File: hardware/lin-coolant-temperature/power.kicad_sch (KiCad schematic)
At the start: 22 parts, among them U4 LTC3203BEDD-PBF, U5 BD9G341EFJ

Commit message: Add firmware for lin-coolant-temperature, cleanup layout
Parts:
- renumbered D2 to D3, R10 to R11, R11 to R12, R12 to R13, R13 to R14, R14 to R15, R15 to R16, R16 to R17, R17 to R18
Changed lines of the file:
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@@
   (symbol (lib_id "power:GND") (at 144.145 89.789 0) (unit 1)
     (in_bom yes) (on_board yes) (fields_autoplaced)
-    (property "Reference" "#PWR030" (id 0) (at 144.145 96.139 0)
+    (property "Reference" "#PWR031" (id 0) (at 144.145 96.139 0)
       (effects (font (size 1.27 1.27)) hide)
     )
@@
   (symbol (lib_id "power:+3V3") (at 100.457 116.967 0) (unit 1)
     (in_bom yes) (on_board yes) (fields_autoplaced)
-    (property "Reference" "#PWR024" (id 0) (at 100.457 120.777 0)
+    (property "Reference" "#PWR025" (id 0) (at 100.457 120.777 0)
       (effects (font (size 1.27 1.27)) hide)
     )
@@
   (symbol (lib_id "power:GND") (at 100.457 152.4 0) (unit 1)
     (in_bom yes) (on_board yes) (fields_autoplaced)
-    (property "Reference" "#PWR025" (id 0) (at 100.457 158.75 0)
+    (property "Reference" "#PWR026" (id 0) (at 100.457 158.75 0)
       (effects (font (size 1.27 1.27)) hide)
     )
@@
   (symbol (lib_id "power:GND") (at 197.358 58.674 0) (unit 1)
     (in_bom yes) (on_board yes) (fields_autoplaced)
-    (property "Reference" "#PWR036" (id 0) (at 197.358 65.024 0)
+    (property "Reference" "#PWR037" (id 0) (at 197.358 65.024 0)
       (effects (font (size 1.27 1.27)) hide)
     )
@@
   (symbol (lib_id "Device:R") (at 106.426 65.278 90) (unit 1)
     (in_bom yes) (on_board yes) (fields_autoplaced)
-    (property "Reference" "R12" (id 0) (at 106.426 59.182 90))
+    (property "Reference" "R13" (id 0) (at 106.426 59.182 90))
     (property "Value" "909k 1%" (id 1) (at 106.426 61.722 90))
     (property "Footprint" "Resistor_SMD:R_0805_2012Metric_Pad1.20x1.40mm_HandSolder" (id 2) (at 106.426 67.056 90)
@@
   (symbol (lib_id "power:+3V3") (at 197.358 41.656 0) (unit 1)
     (in_bom yes) (on_board yes) (fields_autoplaced)
-    (property "Reference" "#PWR035" (id 0) (at 197.358 45.466 0)
+    (property "Reference" "#PWR036" (id 0) (at 197.358 45.466 0)
       (effects (font (size 1.27 1.27)) hide)
     )
@@
   (symbol (lib_id "power:GND") (at 149.098 56.515 0) (unit 1)
     (in_bom yes) (on_board yes) (fields_autoplaced)
-    (property "Reference" "#PWR031" (id 0) (at 149.098 62.865 0)
+    (property "Reference" "#PWR032" (id 0) (at 149.098 62.865 0)
       (effects (font (size 1.27 1.27)) hide)
     )
@@
   (symbol (lib_id "power:+BATT") (at 76.454 51.435 0) (unit 1)
     (in_bom yes) (on_board yes) (fields_autoplaced)
-    (property "Reference" "#PWR019" (id 0) (at 76.454 55.245 0)
+    (property "Reference" "#PWR020" (id 0) (at 76.454 55.245 0)
       (effects (font (size 1.27 1.27)) hide)
     )
@@
   (symbol (lib_id "power:GND") (at 89.027 150.114 0) (unit 1)
     (in_bom yes) (on_board yes) (fields_autoplaced)
-    (property "Reference" "#PWR021" (id 0) (at 89.027 156.464 0)
+    (property "Reference" "#PWR022" (id 0) (at 89.027 156.464 0)
       (effects (font (size 1.27 1.27)) hide)
     )
@@
   (symbol (lib_id "power:GND") (at 170.053 76.2 0) (unit 1)
     (in_bom yes) (on_board yes) (fields_autoplaced)
-    (property "Reference" "#PWR033" (id 0) (at 170.053 82.55 0)
+    (property "Reference" "#PWR034" (id 0) (at 170.053 82.55 0)
       (effects (font (size 1.27 1.27)) hide)
     )
@@
   (symbol (lib_id "power:+5V") (at 198.755 131.191 0) (unit 1)
     (in_bom yes) (on_board yes) (fields_autoplaced)
-    (property "Reference" "#PWR037" (id 0) (at 198.755 135.001 0)
+    (property "Reference" "#PWR038" (id 0) (at 198.755 135.001 0)
       (effects (font (size 1.27 1.27)) hide)
     )
@@
   (symbol (lib_id "power:GND") (at 111.887 156.21 0) (unit 1)
     (in_bom yes) (on_board yes) (fields_autoplaced)
-    (property "Reference" "#PWR027" (id 0) (at 111.887 162.56 0)
+    (property "Reference" "#PWR028" (id 0) (at 111.887 162.56 0)
       (effects (font (size 1.27 1.27)) hide)
     )
@@
   (symbol (lib_id "power:GND") (at 94.488 69.723 0) (unit 1)
     (in_bom yes) (on_board yes) (fields_autoplaced)
-    (property "Reference" "#PWR023" (id 0) (at 94.488 76.073 0)
+    (property "Reference" "#PWR024" (id 0) (at 94.488 76.073 0)
       (effects (font (size 1.27 1.27)) hide)
     )
@@
   (symbol (lib_id "power:GND") (at 198.755 145.669 0) (unit 1)
     (in_bom yes) (on_board yes) (fields_autoplaced)
-    (property "Reference" "#PWR038" (id 0) (at 198.755 152.019 0)
+    (property "Reference" "#PWR039" (id 0) (at 198.755 152.019 0)
       (effects (font (size 1.27 1.27)) hide)
     )
@@
   (symbol (lib_id "power:+3V3") (at 168.275 125.984 0) (unit 1)
     (in_bom yes) (on_board yes) (fields_autoplaced)
-    (property "Reference" "#PWR032" (id 0) (at 168.275 129.794 0)
+    (property "Reference" "#PWR033" (id 0) (at 168.275 129.794 0)
       (effects (font (size 1.27 1.27)) hide)
     )
@@
   (symbol (lib_id "power:GND") (at 111.633 77.089 0) (unit 1)
     (in_bom yes) (on_board yes) (fields_autoplaced)
-    (property "Reference" "#PWR026" (id 0) (at 111.633 83.439 0)
+    (property "Reference" "#PWR027" (id 0) (at 111.633 83.439 0)
       (effects (font (size 1.27 1.27)) hide)
     )
@@
   (symbol (lib_id "Device:R") (at 100.457 145.542 180) (unit 1)
     (in_bom yes) (on_board yes) (fields_autoplaced)
-    (property "Reference" "R11" (id 0) (at 102.616 144.2719 0)
+    (property "Reference" "R12" (id 0) (at 102.616 144.2719 0)
       (effects (font (size 1.27 1.27)) (justify right))
     )
@@
   (symbol (lib_id "power:+12V") (at 94.488 52.705 0) (unit 1)
     (in_bom yes) (on_board yes) (fields_autoplaced)
-    (property "Reference" "#PWR022" (id 0) (at 94.488 56.515 0)
+    (property "Reference" "#PWR023" (id 0) (at 94.488 56.515 0)
       (effects (font (size 1.27 1.27)) hide)
     )
@@
   (symbol (lib_id "Device:R") (at 170.053 70.485 0) (unit 1)
     (in_bom yes) (on_board yes) (fields_autoplaced)
-    (property "Reference" "R17" (id 0) (at 172.339 69.2149 0)
+    (property "Reference" "R18" (id 0) (at 172.339 69.2149 0)
       (effects (font (size 1.27 1.27)) (justify left))
     )
@@
   (symbol (lib_id "power:GND") (at 128.651 80.645 0) (unit 1)
     (in_bom yes) (on_board yes) (fields_autoplaced)
-    (property "Reference" "#PWR028" (id 0) (at 128.651 86.995 0)
+    (property "Reference" "#PWR029" (id 0) (at 128.651 86.995 0)
       (effects (font (size 1.27 1.27)) hide)
     )
@@
   (symbol (lib_id "power:GND") (at 179.705 58.928 0) (unit 1)
     (in_bom yes) (on_board yes) (fields_autoplaced)
-    (property "Reference" "#PWR034" (id 0) (at 179.705 65.278 0)
+    (property "Reference" "#PWR035" (id 0) (at 179.705 65.278 0)
       (effects (font (size 1.27 1.27)) hide)
     )
@@
   (symbol (lib_id "Device:D_Schottky") (at 149.098 50.673 270) (unit 1)
     (in_bom yes) (on_board yes)
-    (property "Reference" "D2" (id 0) (at 154.178 51.308 90)
+    (property "Reference" "D3" (id 0) (at 154.178 51.308 90)
       (effects (font (size 1.27 1.27)) (justify right))
     )
@@
   (symbol (lib_id "Device:R") (at 100.457 123.698 0) (unit 1)
     (in_bom yes) (on_board yes) (fields_autoplaced)
-    (property "Reference" "R10" (id 0) (at 102.235 122.4279 0)
+    (property "Reference" "R11" (id 0) (at 102.235 122.4279 0)
       (effects (font (size 1.27 1.27)) (justify left))
     )
@@
   (symbol (lib_id "power:GND") (at 133.731 89.789 0) (unit 1)
     (in_bom yes) (on_board yes) (fields_autoplaced)
-    (property "Reference" "#PWR029" (id 0) (at 133.731 96.139 0)
+    (property "Reference" "#PWR030" (id 0) (at 133.731 96.139 0)
       (effects (font (size 1.27 1.27)) hide)
     )
@@
   (symbol (lib_id "Device:R") (at 144.145 83.947 0) (unit 1)
     (in_bom yes) (on_board yes) (fields_autoplaced)
-    (property "Reference" "R15" (id 0) (at 146.431 82.6769 0)
+    (property "Reference" "R16" (id 0) (at 146.431 82.6769 0)
       (effects (font (size 1.27 1.27)) (justify left))
     )
@@
   (symbol (lib_id "Device:R") (at 111.633 71.501 0) (unit 1)
     (in_bom yes) (on_board yes) (fields_autoplaced)
-    (property "Reference" "R13" (id 0) (at 114.173 70.2309 0)
+    (property "Reference" "R14" (id 0) (at 114.173 70.2309 0)
       (effects (font (size 1.27 1.27)) (justify left))
     )
@@
   (symbol (lib_id "Device:R") (at 133.731 84.074 0) (unit 1)
     (in_bom yes) (on_board yes) (fields_autoplaced)
-    (property "Reference" "R14" (id 0) (at 136.271 82.8039 0)
+    (property "Reference" "R15" (id 0) (at 136.271 82.8039 0)
       (effects (font (size 1.27 1.27)) (justify left))
     )
@@
   (symbol (lib_id "Device:R") (at 170.053 53.848 0) (unit 1)
     (in_bom yes) (on_board yes) (fields_autoplaced)
-    (property "Reference" "R16" (id 0) (at 172.339 52.5779 0)
+    (property "Reference" "R17" (id 0) (at 172.339 52.5779 0)
       (effects (font (size 1.27 1.27)) (justify left))
     )
@@
   (symbol (lib_id "power:+3V3") (at 89.027 128.27 0) (unit 1)
     (in_bom yes) (on_board yes) (fields_autoplaced)
-    (property "Reference" "#PWR020" (id 0) (at 89.027 132.08 0)
-      (effects (font (size 1.27 1.27)) hide)
-    )
+    (property "Reference" "#PWR021" (id 0) (at 89.027 132.08 0)
+      (effects (font (size 1.27 1.27)) hide)
+    )

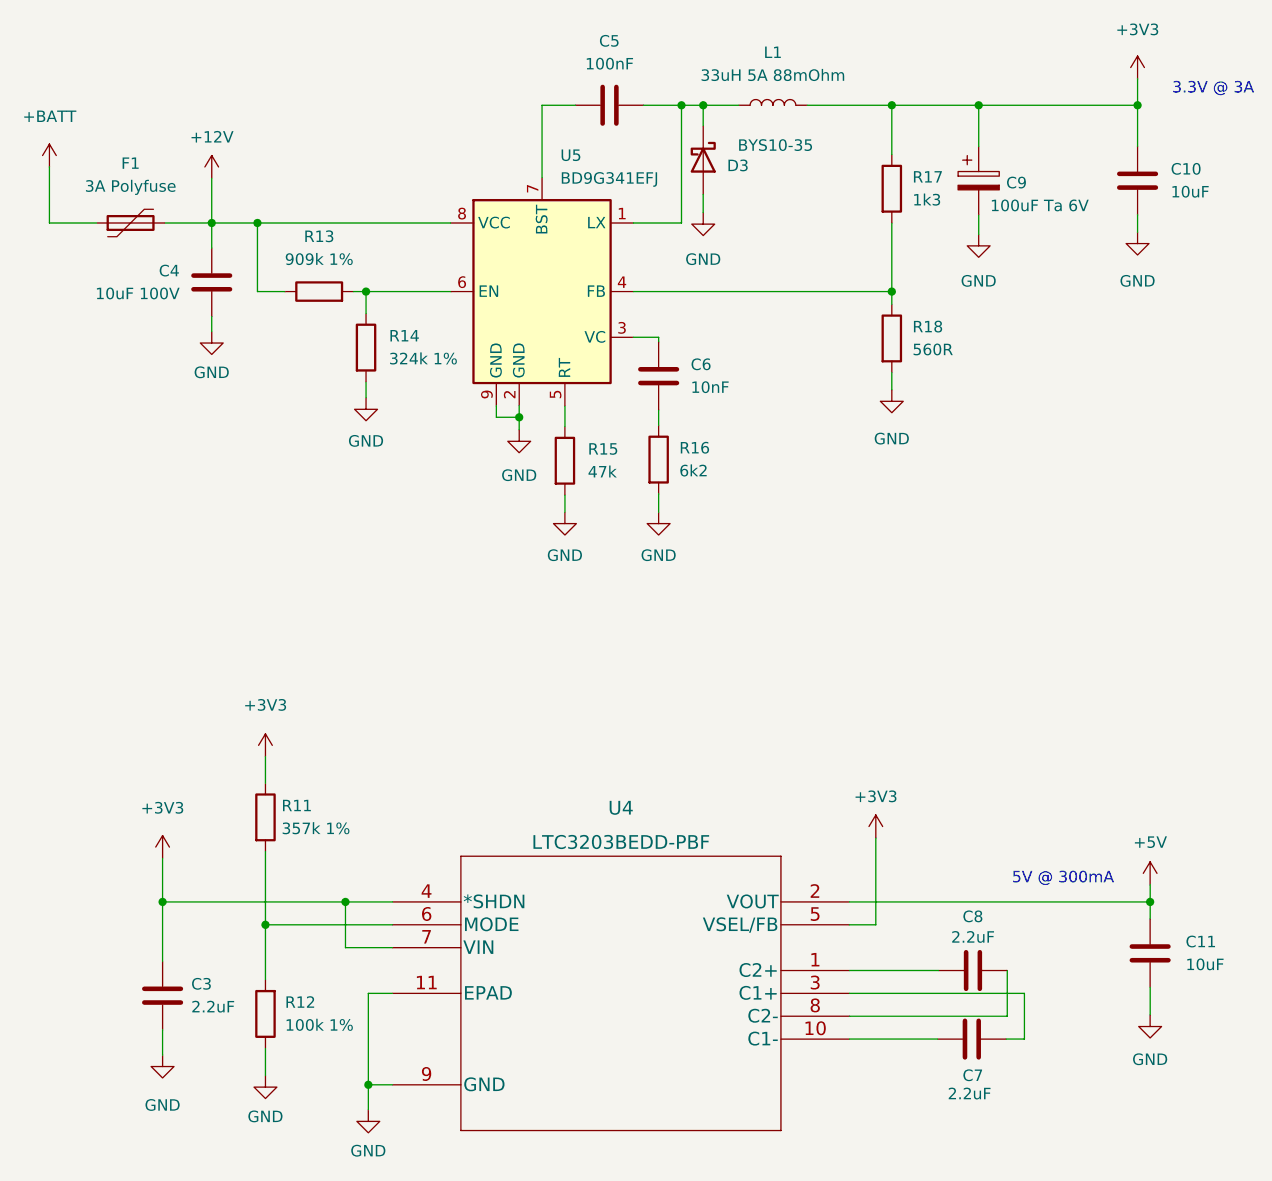
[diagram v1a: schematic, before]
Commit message: Update the schematics... remove PCA9536, use voltage regulator
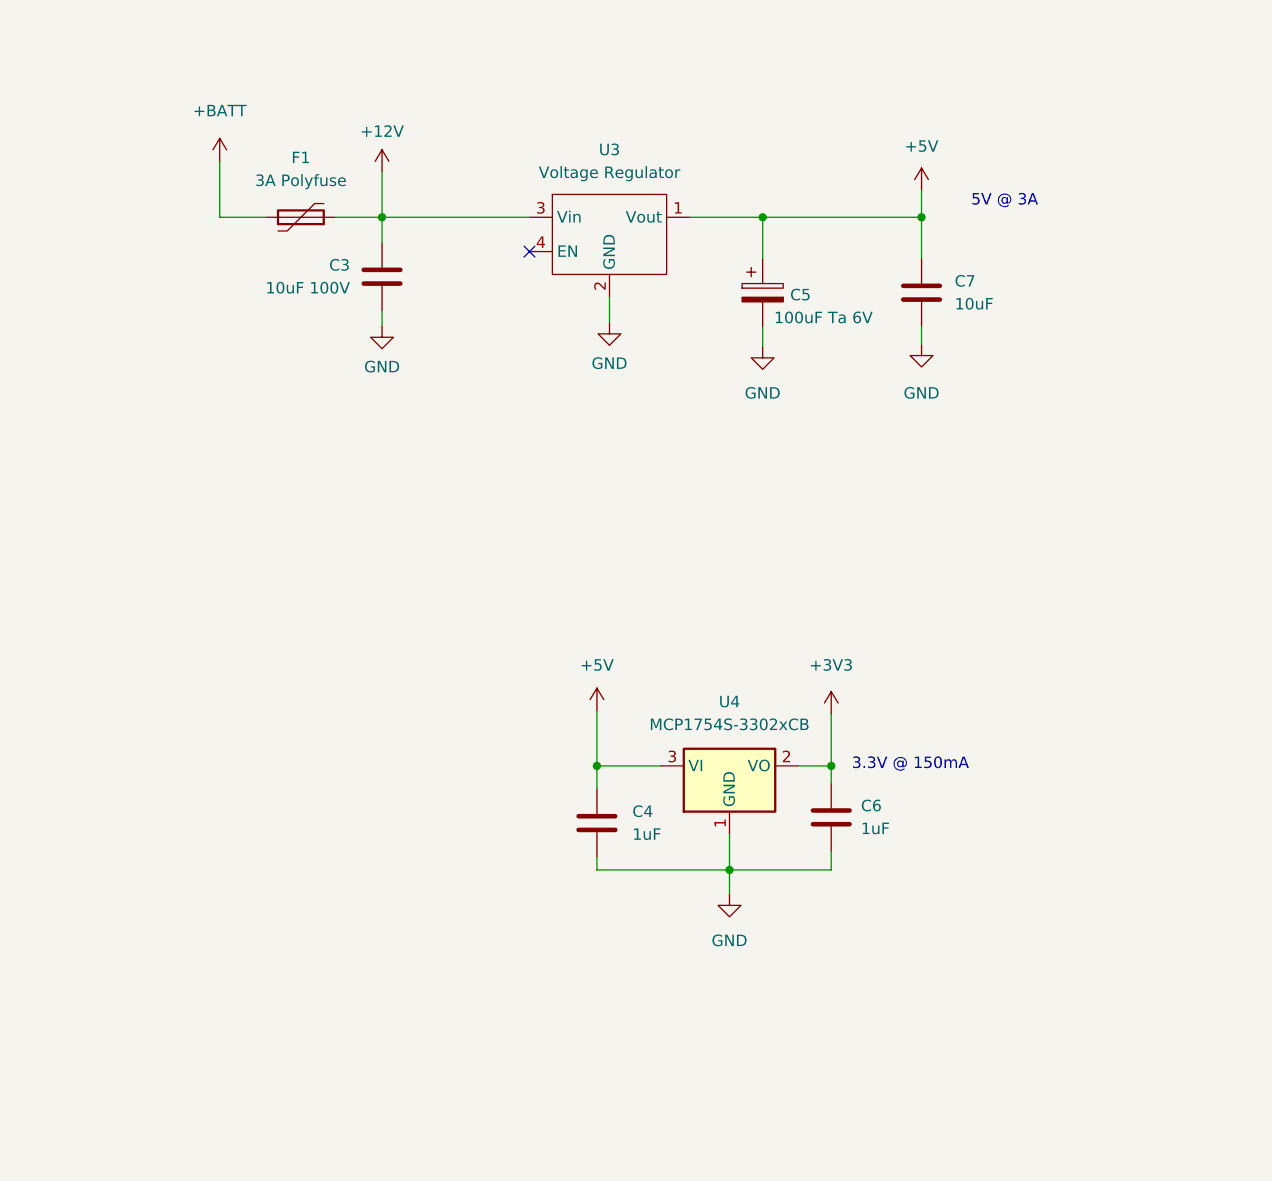
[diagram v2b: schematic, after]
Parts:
- removed C10, C11: 10uF, Capacitor_SMD:C_0805_2012Metric_Pad1.18x1.45mm_HandSolder, symbol Device:C
- removed C5: 100nF, Capacitor_SMD:C_0805_2012Metric_Pad1.18x1.45mm_HandSolder, symbol Device:C
- removed C8: 2.2uF, Capacitor_SMD:C_0805_2012Metric_Pad1.18x1.45mm_HandSolder, symbol Device:C
- removed C9: 100uF Ta 6V, Capacitor_Tantalum_SMD:CP_EIA-3216-10_Kemet-I_Pad1.58x1.35mm_HandSolder, symbol Device:C_Polarized
- removed D3: BYS10-35, Diode_SMD:D_SMA_Handsoldering, symbol Device:D_Schottky
- removed L1: 33uH 5A 88mOhm, Beirdo:PM4346.333NLT, symbol Device:L
- removed R11: 357k 1%, Resistor_SMD:R_0805_2012Metric_Pad1.20x1.40mm_HandSolder, symbol Device:R
- removed R12: 100k 1%, Resistor_SMD:R_0805_2012Metric_Pad1.20x1.40mm_HandSolder, symbol Device:R
- removed R13: 909k 1%, Resistor_SMD:R_0805_2012Metric_Pad1.20x1.40mm_HandSolder, symbol Device:R
- removed R14: 324k 1%, Resistor_SMD:R_0805_2012Metric_Pad1.20x1.40mm_HandSolder, symbol Device:R
- removed R15: 47k, Resistor_SMD:R_0805_2012Metric_Pad1.20x1.40mm_HandSolder, symbol Device:R
- removed R16: 6k2, Resistor_SMD:R_0805_2012Metric_Pad1.20x1.40mm_HandSolder, symbol Device:R
- removed R17: 1k3, Resistor_SMD:R_0805_2012Metric_Pad1.20x1.40mm_HandSolder, symbol Device:R
- removed R18: 560R, Resistor_SMD:R_0805_2012Metric_Pad1.20x1.40mm_HandSolder, symbol Device:R
- removed U4: LTC3203BEDD-PBF, UltraLibrarian:LTC3203BEDD-PBF, symbol UltraLibrarian:LTC3203BEDD-PBF
- removed U5: BD9G341EFJ, Package_SO:HTSOP-8-1EP_3.9x4.9mm_P1.27mm_EP2.4x3.2mm_ThermalVias, symbol Beirdo:BD9G341EFJ
- added C5: 100uF Ta 6V, Capacitor_Tantalum_SMD:CP_EIA-3216-10_Kemet-I_Pad1.58x1.35mm_HandSolder, symbol Device:C_Polarized
- added U3: Voltage Regulator, Beirdo:Switching_Regulator_Module, symbol Beirdo:Switching_Regulator_Module
- added U4: MCP1754S-3302xCB, Package_TO_SOT_SMD:SOT-23, symbol Regulator_Linear:MCP1754S-3302xCB
- C3: value 2.2uF -> 10uF 100V; footprint Capacitor_SMD:C_0805_2012Metric_Pad1.18x1.45mm_HandSolder -> Capacitor_SMD:C_1210_3225Metric_Pad1.33x2.70mm_HandSolder
- C4: value 10uF 100V -> 1uF; footprint Capacitor_SMD:C_1210_3225Metric_Pad1.33x2.70mm_HandSolder -> Capacitor_SMD:C_0805_2012Metric_Pad1.18x1.45mm_HandSolder
- C6: value 10nF -> 1uF
- C7: value 2.2uF -> 10uF
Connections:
- net +12V: now also C3.1, U3.3 (Vin); no longer C4.1
- net +3V3: now also C6.1, U4.2 (VO); no longer C3.1
- net +5V: now also C4.1, C7.1, C5.1, U3.1 (Vout), U4.3 (VI)
- net GND: now also C6.2, C7.2, C5.2, U3.2 (GND), U4.1 (GND)
- no-connect marks 0 -> 1
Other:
- note added: "3.3V @ 150mA"
- note added: "5V @ 3A"
- note removed: "3.3V @ 3A"
- note removed: "5V @ 300mA"
